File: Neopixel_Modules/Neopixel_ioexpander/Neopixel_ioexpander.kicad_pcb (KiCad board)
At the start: 2 copper layers, 39.6 x 33.2 mm, 15 parts, among them J1 PINHD_1x16_Male, J2 PINHD_1x4_Male, J3 PINHD_1x4_Male, SW2 SW_DIP_x03

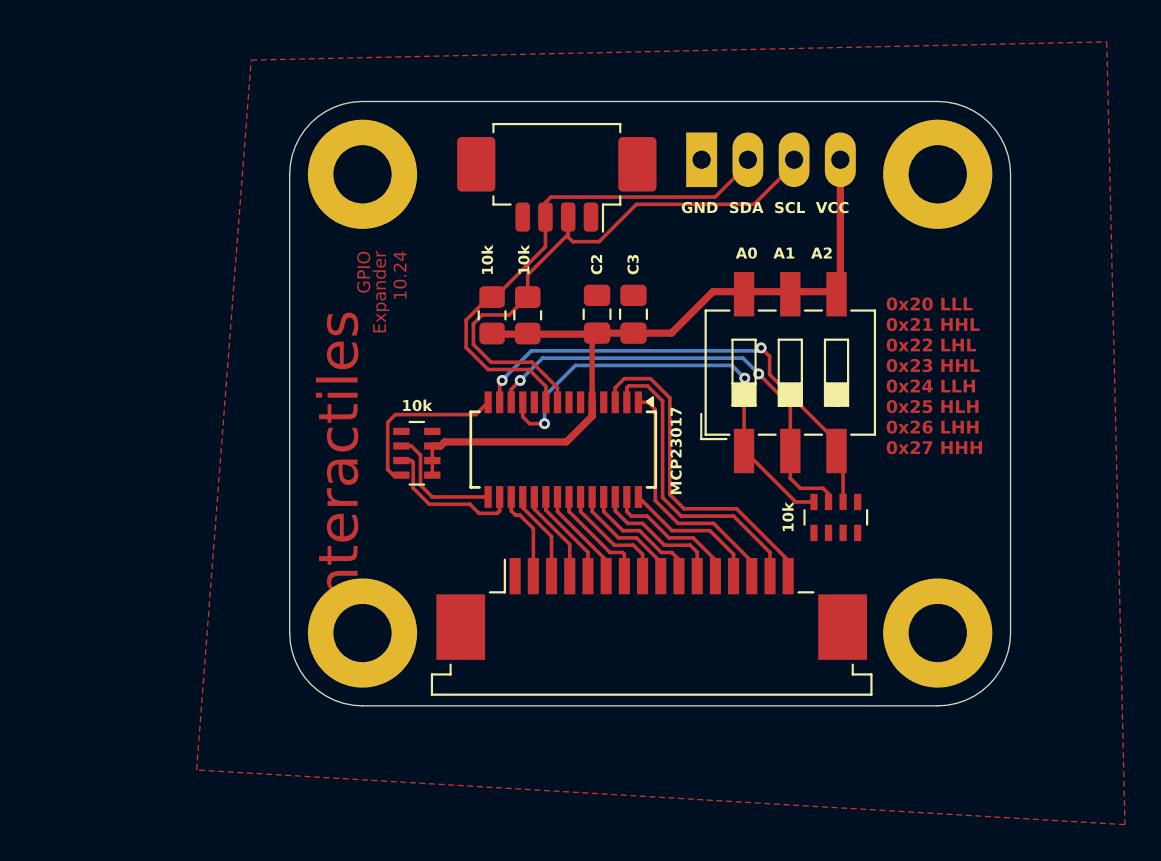
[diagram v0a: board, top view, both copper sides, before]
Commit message: updated IO expander to bigger MCP23017 footprint
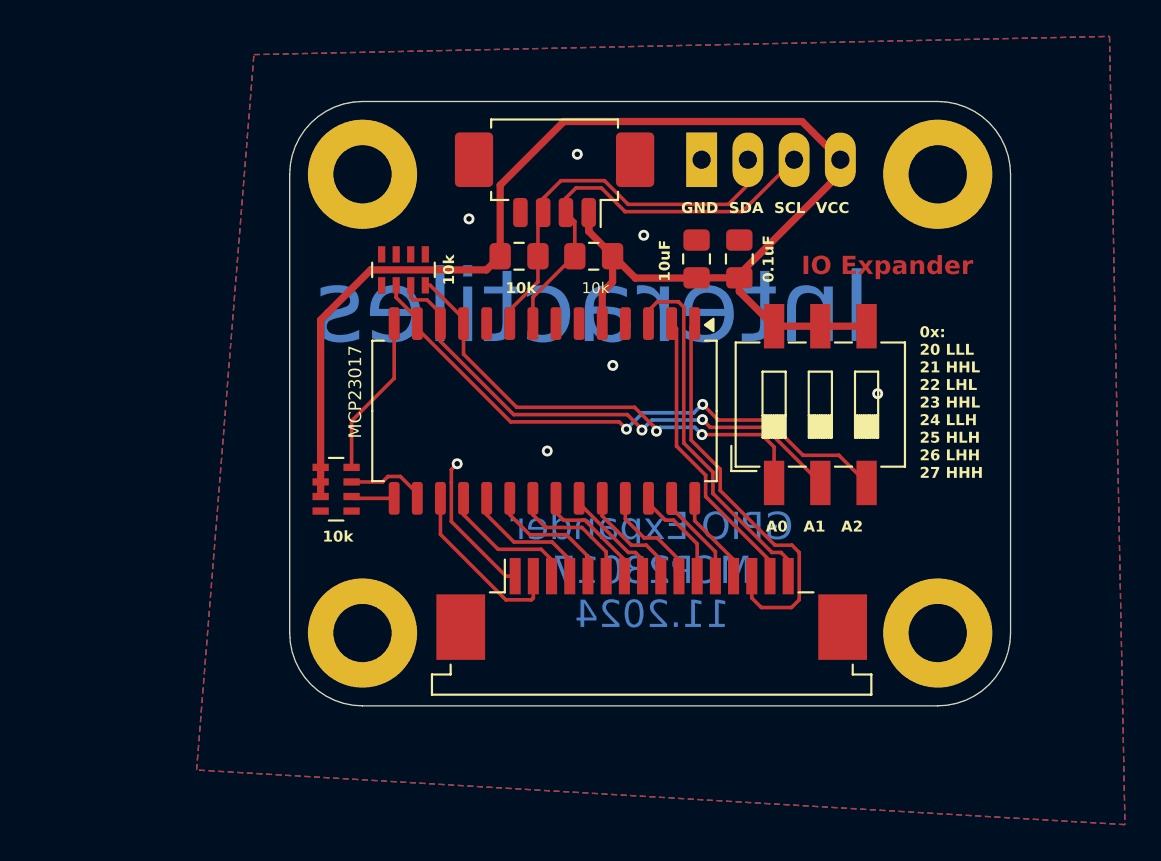
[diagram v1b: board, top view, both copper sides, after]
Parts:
- removed the 10k at (79.1, 85.2)
- removed the 10k at (102.1, 88.7)
- added 10k: R_Pack04, Resistor_SMD:R_Array_Concave_4x0603, F.Cu at (74.7, 87.2)
- added 10k: R_Pack04, Resistor_SMD:R_Array_Concave_4x0603, F.Cu at (78.4, 75.1)
- 10k: renamed from R4; footprint Resistor_SMD:R_0805_2012Metric_Pad1.20x1.40mm_HandSolder -> Capacitor_SMD:C_0805_2012Metric_Pad1.18x1.45mm_HandSolder
- 10k: renamed from R5; footprint Resistor_SMD:R_0805_2012Metric_Pad1.20x1.40mm_HandSolder -> Capacitor_SMD:C_0805_2012Metric_Pad1.18x1.45mm_HandSolder
- MCP23017: footprint Package_SO:SSOP-28_3.9x9.9mm_P0.635mm -> Package_SO:SOIC-28W_7.5x18.7mm_P1.27mm
- moved 0.1uF 6.56 mm to (96.8, 74.5)
- moved 10uF 6.25 mm to (94.5, 74.5)
- moved 10k 4.86 mm to (88.8, 74.4), turned to 0 degrees
- moved 10k 3.57 mm to (84.7, 74.4), turned to 180 degrees
- moved SW2 2.41 mm to (101.3, 82.5)
- moved MCP23017 2.36 mm to (86.1, 82.9)
- moved J2 0.28 mm to (86.7, 69.6)
- renumbered C3 to 0.1uF, C2 to 10uF
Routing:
- net VCC: track 42.8 -> 78.5 mm
- net SCL: track 31.8 -> 22.5 mm
- net SW13: track 13.6 -> 22.5 mm
- net GND: track 0.00 -> 8.06 mm, vias 0 -> 7
- net SDA: track 28.1 -> 21.6 mm
- net Net-(RN2-R3.2): track 26.6 -> 32.2 mm
- net SW1: track 5.00 -> 9.82 mm
- net Net-(RN1-R2.1): track 6.94 -> 2.38 mm
- net Net-(RN2-R2.2): track 24.7 -> 28.8 mm
- net Net-(RN1-R3.1): track 8.30 -> 4.39 mm
- net SW2: track 5.00 -> 7.66 mm
- net SW12: track 7.73 -> 5.16 mm
- net SW11: track 7.65 -> 5.27 mm
- net SW3: track 5.16 -> 7.39 mm
- net SW4: track 5.31 -> 7.23 mm
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- added copper zone on B.Cu, net GND
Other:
- board text added: "0x: 20 LLL 21 HHL 22 LHL 23 HHL 24 LLH 25 HLH 26 LHH 27 HHH"
- board text added: "GPIO Expander MCP23017 11.2024"
- board text added: "IO Expander"
- board text added: "VCC SCL SDA GND"
- board text removed: "0x20 LLL 0x21 HHL 0x22 LHL 0x23 HHL 0x24 LLH 0x25 HLH 0x26 LHH 0x27 HHH"
- board text removed: "Expander 10.24"
- board text removed: "GPIO"

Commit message: fixed for pcb production
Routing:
- net GND: track 8.06 -> 4.06 mm
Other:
- board text added: "I/O Expander"
- board text removed: "IO Expander"

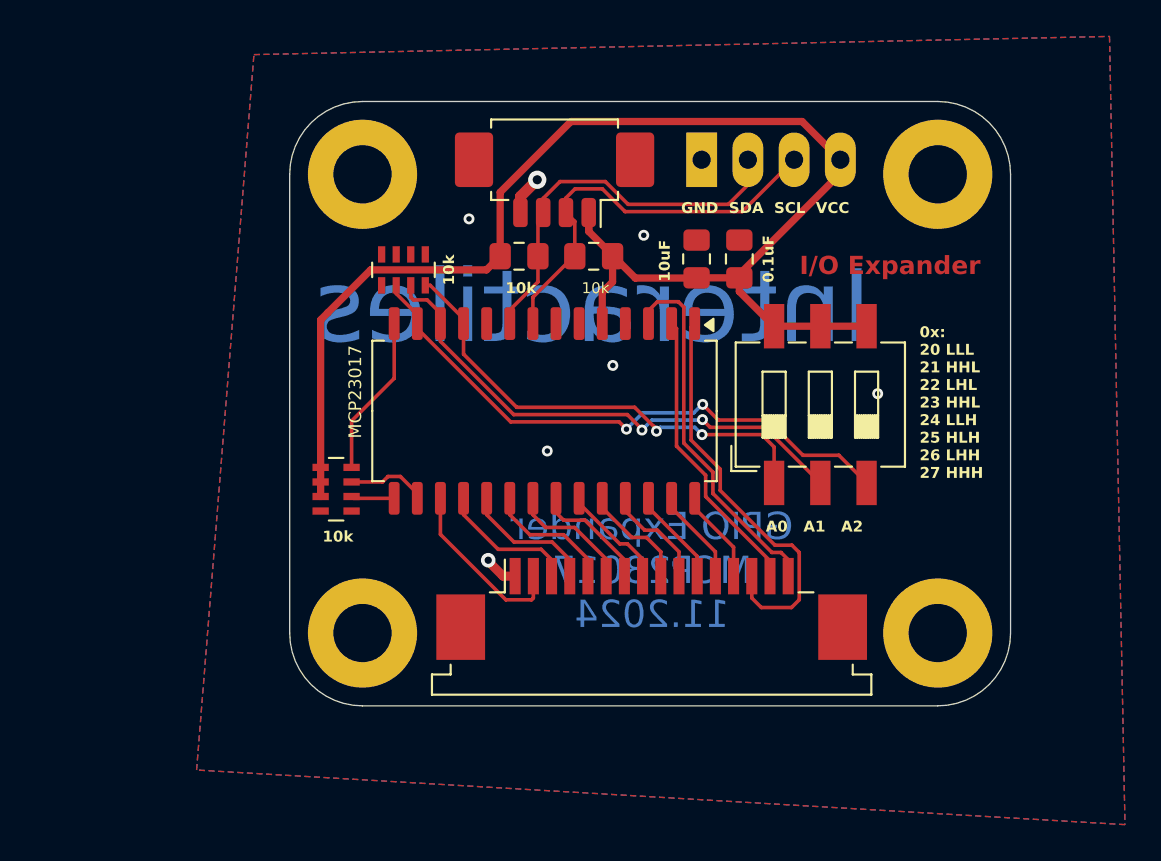
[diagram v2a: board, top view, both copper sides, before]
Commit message: PCB Revisions
MCP23017 had incorrect footprints, some tolerances between pads were too tight (shorts), resized some components
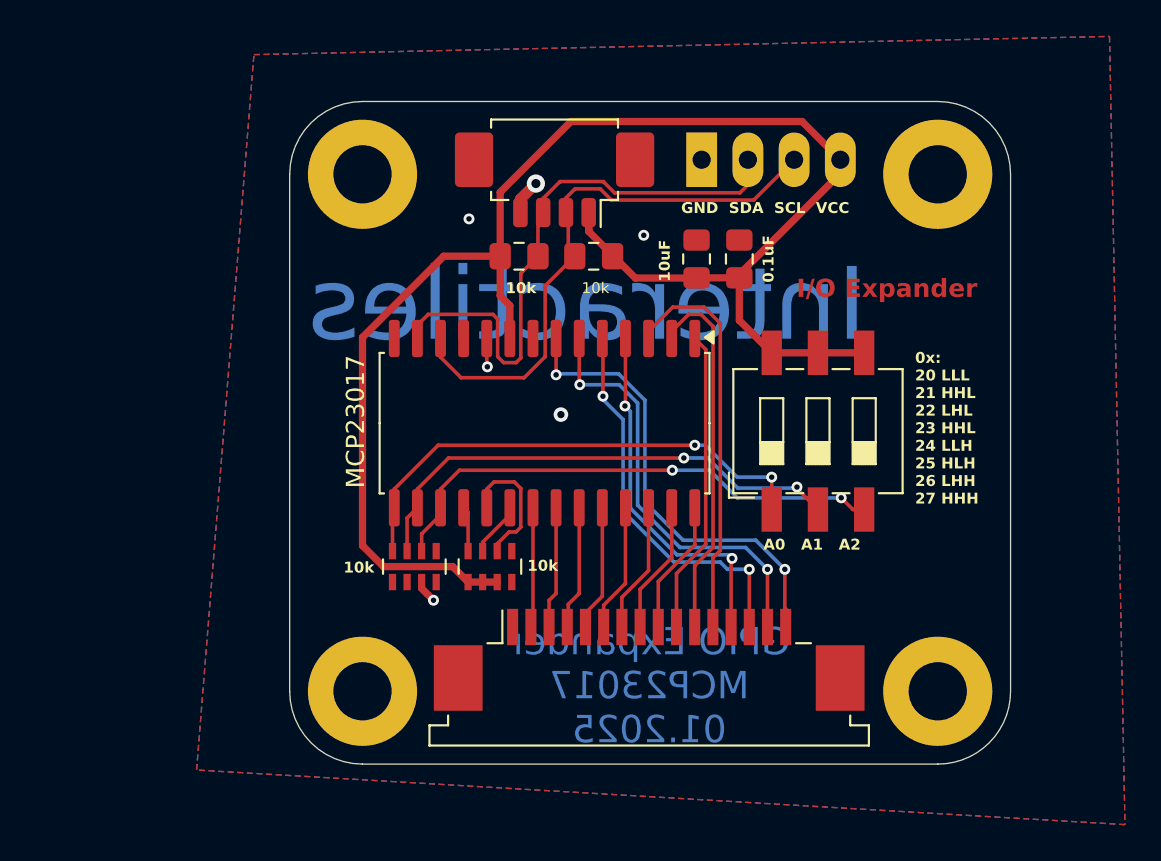
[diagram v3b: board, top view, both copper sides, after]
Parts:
- MCP23017: value MCP23017_ML -> MCP23017_SO; footprint Package_SO:SOIC-28W_7.5x18.7mm_P1.27mm -> Package_SO:SOIC-28W_7.5x17.9mm_P1.27mm
- moved 10k 16.3 mm to (79.0, 91.4), turned to 90 degrees
- moved 10k 9.46 mm to (83.1, 91.4), turned to -90 degrees
- moved H1 3.20 mm to (76.1, 98.3)
- moved H2 3.20 mm to (107.7, 98.3)
- moved J1 2.80 mm to (91.9, 96.5)
- moved SW2 1.47 mm to (101.1, 84.0)
- moved MCP23017 0.67 mm to (86.1, 83.5)
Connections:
- MCP23017 pad 1: SW13 -> SW9
- MCP23017 pad 10: unconnected-(U3-NC-Pad10) -> GND
- MCP23017 pad 11: Net-(RN2-R1.2) -> unconnected-(U3-NC-Pad11)
- MCP23017 pad 12: Net-(RN2-R2.2) -> SCL
- MCP23017 pad 13: Net-(RN2-R3.2) -> SDA
- MCP23017 pad 14: Net-(RN1-R4.1) -> unconnected-(U3-NC-Pad14)
- MCP23017 pad 15: Net-(RN1-R2.1) -> Net-(RN2-R1.2)
- MCP23017 pad 16: Net-(RN1-R3.1) -> Net-(RN2-R2.2)
- MCP23017 pad 17: SW1 -> Net-(RN2-R3.2)
- MCP23017 pad 18: SW2 -> Net-(RN1-R4.1)
- MCP23017 pad 19: SW3 -> Net-(RN1-R2.1)
- MCP23017 pad 2: SW14 -> SW10
- MCP23017 pad 20: SW4 -> Net-(RN1-R3.1)
- MCP23017 pad 21: SW5 -> SW1
- MCP23017 pad 22: SW6 -> SW2
- MCP23017 pad 23: SW7 -> SW3
- MCP23017 pad 24: SW8 -> SW4
- MCP23017 pad 25: SW9 -> SW5
- MCP23017 pad 26: SW10 -> SW6
- MCP23017 pad 27: SW11 -> SW7
- MCP23017 pad 28: SW12 -> SW8
- MCP23017 pad 3: SW15 -> SW11
- MCP23017 pad 4: unconnected-(U3-GPB7-Pad4) -> SW12
- MCP23017 pad 5: VCC -> SW13
- MCP23017 pad 6: GND -> SW14
- MCP23017 pad 7: unconnected-(U3-NC-Pad7) -> SW15
- MCP23017 pad 8: SCL -> unconnected-(U3-GPB7-Pad8)
- MCP23017 pad 9: SDA -> VCC
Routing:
- net SW11: track 5.27 -> 22.1 mm
- net SW10: track 5.38 -> 20.3 mm
- net SW12: track 5.16 -> 20.0 mm, vias 0 -> 2
- net SW9: track 5.90 -> 16.8 mm
- net VCC: track 78.3 -> 88.5 mm
- net SDA: track 21.6 -> 31.8 mm
- net SCL: track 22.5 -> 31.2 mm
- net SW14: track 16.1 -> 24.4 mm, vias 0 -> 2
- net Net-(RN1-R4.1): track 8.87 -> 2.48 mm
- net SW15: track 20.4 -> 25.5 mm, vias 0 -> 2
- net Net-(RN1-R2.1): track 2.38 -> 7.41 mm
- net Net-(RN2-R3.2): track 32.2 -> 28.4 mm
- net SW1: track 9.82 -> 6.60 mm
- net Net-(RN2-R1.2): track 26.2 -> 27.7 mm
- net Net-(RN1-R3.1): track 4.39 -> 3.00 mm
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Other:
- board size 39.6 x 33.2 mm -> 39.6 x 36.4 mm
- board text added: "GPIO Expander MCP23017 01.2025"
- board text removed: "GPIO Expander MCP23017 11.2024"
